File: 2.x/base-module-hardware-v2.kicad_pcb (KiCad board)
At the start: 4 copper layers, 99.7 x 99.7 mm, 275 parts, among them K1 CONN_3, P1 PINBALL-CONNECTOR, P2 PINBALL-CONNECTOR, P3 SOLENOID-CONNECTOR, P4 CONN_16, P5 CONN_16, P6 HE10-32, Q1 BC846, Q10 DMN6040SSD, Q11 BC846, Q12 BC846, Q13 DMP2240UDM, Q14 DMP2240UDM, Q15 BC846, Q16 BC846, Q17 BC846, Q18 BC846, Q19 DMN6040SSD, Q2 BC846, Q20 DMN6040SSD, Q21 BC846, Q22 BC846, Q23 BC846, Q24 BC846, Q25 BC846, Q26 BC846, Q27 BC846, Q28 BC846, Q29 BSS138, Q3 DMN6040SSD, Q30 FDD5614P, Q31 BC846, Q32 BSS138, Q4 DMN6040SSD, Q5 BC846, Q6 BC846, Q7 BC846, Q8 BC846, Q9 DMN6040SSD, U1 74LVC14, U2 STM32F072R, U3 MCP2562, U4 MC78L05ACH, U5 AP1117IE33G, U6 ZXCT1086E5TA, U7 ZXCT1107SA-7, U8 LM7805CT, U9 MMA8653FC, X1 8.000 MHz

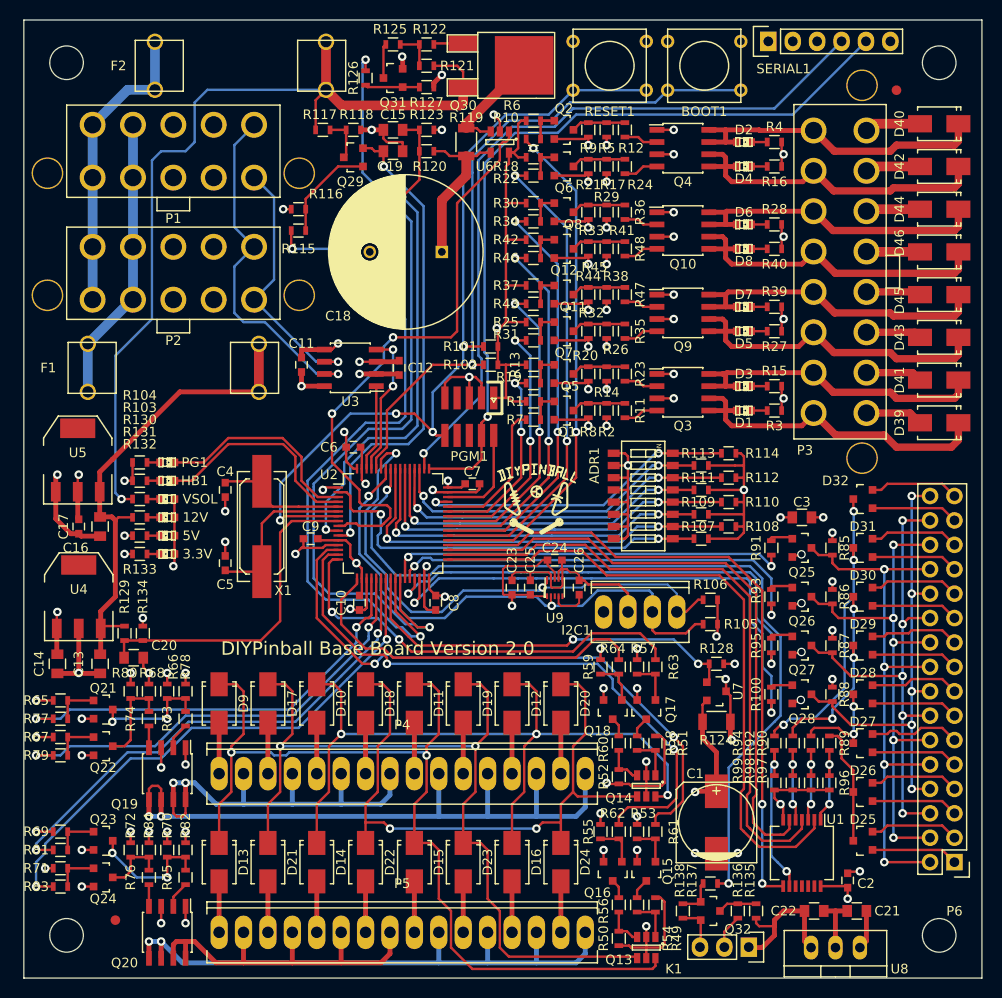
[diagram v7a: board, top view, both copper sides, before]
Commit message: Fixing BAT54C pinout, and some feedback from layout review.
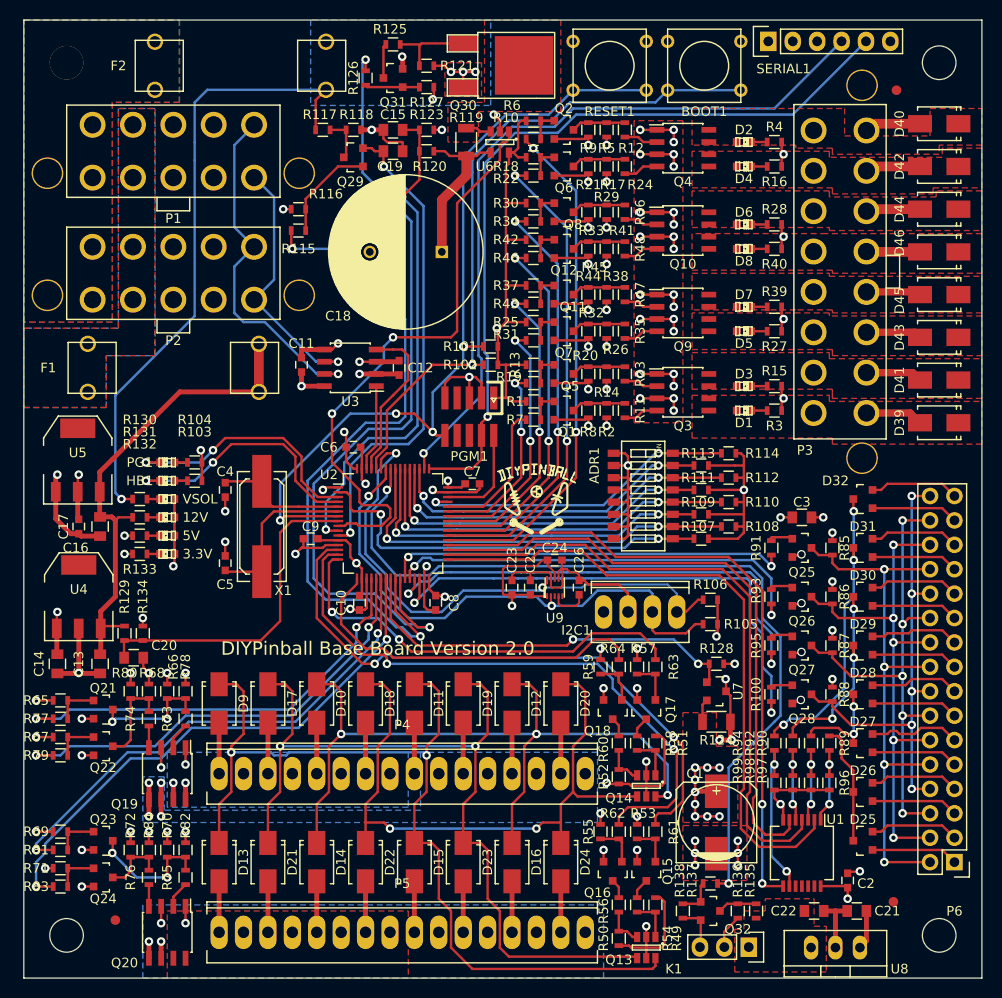
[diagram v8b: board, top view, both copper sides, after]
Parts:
- removed R122: 22, Resistors_SMD:R_0603
- added FIDUCIAL: VAL**, PinballParts:FIDUCIAL, F.Cu at (146.4, 171.8)
- moved R103 5.72 mm to (73.7, 128.0), turned to 0 degrees
- moved R104 5.72 mm to (73.7, 126.0), turned to 0 degrees
- turned HB1 to 0 degrees
- turned PG1 to 0 degrees
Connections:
- R121 pad 2: Net-(R121-Pad2) -> Net-(Q30-PadG)
- R125 pad 1: Net-(R121-Pad2) -> Net-(Q30-PadG)
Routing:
- net Net-(P4-Pad10): track 69.9 -> 6.99 mm, vias 2 -> 4
- net Net-(P5-Pad10): track 62.0 -> 3.50 mm
- net Net-(P4-Pad2): track 43.5 -> 3.50 mm
- net Net-(P5-Pad2): track 38.9 -> 0.00 mm
- net Net-(D1-Pad2): track 35.4 -> 0.00 mm
- net Net-(D43-Pad1): track 35.2 -> 0.00 mm
- net Net-(D4-Pad2): track 34.6 -> 0.00 mm
- net Net-(D46-Pad1): track 34.7 -> 0.09 mm
- net Net-(D45-Pad1): track 33.6 -> 0.00 mm
- net Net-(D2-Pad2): track 33.3 -> 0.00 mm
- net Net-(D3-Pad2): track 33.3 -> 0.00 mm
- net Net-(D44-Pad1): track 33.0 -> 0.00 mm
- net /Power Supply/VSOL_IN: track 31.2 -> 0.00 mm
- net /Power Supply/12V_IN: track 29.8 -> 0.00 mm
- net GND: track 248.1 -> 277.4 mm, vias 67 -> 87
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- added copper zone on F.Cu, net /Lamp Driver/LAMP_12V
- added copper zone on B.Cu, net /Power Supply/12V_IN
- added copper zone on F.Cu, net /Power Supply/12V_IN
- added copper zone on B.Cu, net /Power Supply/VSOL_IN
- added copper zone on F.Cu, net /Power Supply/VSOL_IN
- added copper zone on F.Cu, net GND
- added copper zone on F.Cu, net Net-(C22-Pad1)
- added copper zone on F.Cu, net Net-(D1-Pad2)
- added copper zone on F.Cu, net Net-(D2-Pad2)
- added copper zone on F.Cu, net Net-(D3-Pad2)
- added copper zone on F.Cu, net Net-(D4-Pad2)
- added copper zone on F.Cu, net Net-(D43-Pad1)
- added copper zone on F.Cu, net Net-(D44-Pad1)
- added copper zone on F.Cu, net Net-(D45-Pad1)
- added copper zone on F.Cu, net Net-(D46-Pad1)
- added copper zone on B.Cu, net Net-(P4-Pad10)
- added copper zone on B.Cu, net Net-(P4-Pad2)
- added copper zone on B.Cu, net Net-(P5-Pad10)
- added copper zone on F.Cu, net Net-(P5-Pad2)
- added copper zone on F.Cu, net Net-(Q30-PadD)
- added copper zone on B.Cu, net VEE
- added copper zone on F.Cu, net VEE
